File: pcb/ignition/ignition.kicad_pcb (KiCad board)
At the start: 2 copper layers, 71 parts, among them IC1 LTC4151, IC2 LTC4151, IC3 LTC4151, IC4 LTC4151, IC5 LTC4151, IC6 LTC4151, IC7 STM32F4xxVxTx, J1 PSU, J2 PSU, J3 CH2, J4 CH4, J5 CH1, J6 CH3, J7 CH5, Q1 NFET, Q2 NFET, Q3 NFET, Q4 NFET, Q5 NFET, Q6 NFET

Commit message: finished schematic
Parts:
- added C1: 10u, agg:1206, F.Cu at (67.4, -17.0)
- added C10: 100n, agg:0402, F.Cu at (122.8, -16.2)
- added C11: 100n, agg:0402, F.Cu at (149.0, -34.7)
- added C12: 1µ, agg:0402, F.Cu at (145.2, -29.2)
- added C13: 100n, agg:0402, F.Cu at (149.0, -33.5)
- added C14: 100n, agg:0402, F.Cu at (145.9, -30.5)
- added C15: 100n, agg:0402, F.Cu at (152.1, -37.1)
- added C16: 100n, agg:0402, F.Cu at (134.6, -18.9)
- added C17: 2µ2, agg:0402, F.Cu at (140.6, -42.2)
- added C18: 2µ2, agg:0402, F.Cu at (155.8, -40.6)
- added C19: 100n, agg:0402, F.Cu at (120.7, -16.2)
- added C2: 10u, agg:1206, F.Cu at (72.1, -17.0)
- added C20: 100n, agg:0402, F.Cu at (118.6, -16.2)
- added C3: 1u, agg:0603-L, F.Cu at (140.7, -44.5)
- added C4: 10n, agg:0603-L, F.Cu at (140.7, -43.4)
- added C5: 1u, agg:0603-L, F.Cu at (122.7, -35.2)
- added C6: 10p, agg:0402, F.Cu at (124.9, -16.2)
- added C7: 10p, agg:0402, F.Cu at (127.0, -16.2)
- added C8: 4µ7, agg:0402, F.Cu at (129.2, -16.2)
- added C9: 100n, agg:0402, F.Cu at (145.9, -31.7)
- added D12: D, ignition:SOD-123F, F.Cu at (137.5, -45.0)
- added D13: D, ignition:SOD-123F, F.Cu at (137.5, -42.7)
- added IC8: STM32F437VIT6, agg:LQFP-100, F.Cu at (88.0, 42.0)
- added J10: CH2, ignition:172316-1104, F.Cu at (54.0, 114.0)
- added J11: CH4, ignition:172316-1104, F.Cu at (94.0, 114.0)
- added J12: ARM, agg:S02B-PASK-2, F.Cu at (111.0, 42.0)
- added J13: UART1, agg:S03B-PASK-2, F.Cu at (111.0, 34.0)
- added J14: UART2, agg:S03B-PASK-2, F.Cu at (111.0, 25.0)
- added J15: CH1, ignition:172316-1104, F.Cu at (34.0, 114.0)
- added J16: CH3, ignition:172316-1104, F.Cu at (74.0, 114.0)
- added J17: CH5, ignition:172316-1104, F.Cu at (114.0, 114.0)
- added J8: LED4, agg:S02B-PASK-2, F.Cu at (85.0, 111.0)
- added J9: LED5, agg:S02B-PASK-2, F.Cu at (105.0, 111.0)
- added K1: 16A SPST, ignition:RT33L024, F.Cu at (68.0, -56.0)
- added K2: 16A SPST, ignition:RT33L024, F.Cu at (99.0, -69.5)
- added K3: 16A SPST, ignition:RT33L024, F.Cu at (68.0, -42.5)
- added K4: 16A SPST, ignition:RT33L024, F.Cu at (99.0, -56.0)
- added K5: 16A SPST, ignition:RT33L024, F.Cu at (68.0, -69.5)
- added K6: 16A SPST, ignition:RT33L024, F.Cu at (53.0, -77.0)
- added P1: SWD_TC, agg:TC2030-NL, F.Cu at (92.2, -24.0)
- added R41: 1k, agg:0603, F.Cu at (135.1, -21.7)
- added R42: 100R, agg:0603, F.Cu at (153.2, -40.0)
- added R43: 100R, agg:0603, F.Cu at (132.0, -20.2)
- added R44: 100R, agg:0603, F.Cu at (132.0, -18.7)
- added R45: 1k, agg:0603, F.Cu at (160.0, -48.0)
- added R46: 100R, agg:0603, F.Cu at (174.7, -62.5)
- added R47: 1k, agg:0603, F.Cu at (135.1, -20.2)
- added R48: 1k, agg:0603, F.Cu at (132.0, -17.2)
- added R49: 1k, agg:0603, F.Cu at (156.9, -42.0)
- added R50: 1k, agg:0603, F.Cu at (160.0, -45.0)
- added R51: 1k, agg:0603, F.Cu at (138.9, -24.0)
- added R52: 10k, agg:0603, F.Cu at (142.6, -27.5)
- added R53: 10k, agg:0603, F.Cu at (138.9, -25.5)
- added R54: 10k, agg:0603, F.Cu at (174.7, -67.0)
- added R55: 47k, agg:0603-L, F.Cu at (140.7, -45.6)
- added R56: 47k, agg:0603-L, F.Cu at (155.5, -62.1)
- added R57: 47k, agg:0603-L, F.Cu at (155.5, -63.2)
- added R58: 47k, agg:0603-L, F.Cu at (155.7, -64.3)
- added R59: 47k, agg:0603-L, F.Cu at (114.2, -16.3)
- added R60: 100, agg:0402, F.Cu at (116.5, -16.2)
- added TP1: TESTPAD, agg:TESTPAD, F.Cu at (136.3, -40.7)
- added TP2: TESTPAD, agg:TESTPAD, F.Cu at (179.1, -79.2)
- added TP3: TESTPAD, agg:TESTPAD, F.Cu at (129.5, -35.1)
- added TP4: TESTPAD, agg:TESTPAD, F.Cu at (179.1, -76.2)
- added TP5: TESTPAD, agg:TESTPAD, F.Cu at (179.1, -77.7)
- added U1: MICROSD, agg:MICROSD_MOLEX_503398-1892, F.Cu at (134.4, -69.2)
- added X33: Hole, agg:M3_MOUNT, F.Cu at (133.8, -36.2)
- added X34: Hole, agg:M3_MOUNT, F.Cu at (152.0, -45.6)
- added X35: Hole, agg:M3_MOUNT, F.Cu at (133.8, -29.4)
- added X36: Hole, agg:M3_MOUNT, F.Cu at (160.5, -52.2)
- added Y1: 26M, agg:XTAL-20x16, F.Cu at (155.7, -66.3)
- D10, D9: value D -> LED; footprint ignition:SOD-123F -> agg:0603-LED
- IC7: value STM32F4xxVxTx -> ADP3335; footprint agg:LQFP-100 -> agg:MSOP-8
- J1: footprint agg:S03B-PASK-2 -> ignition:172316-1104
- J2: value PSU -> LED1; footprint agg:S03B-PASK-2 -> agg:S02B-PASK-2
- J3: value CH2 -> PSU; footprint agg:S02B-PASK-2 -> ignition:172316-1104
- J4: value CH4 -> LED2
- J5: value CH1 -> 5v In
- J6: value CH3 -> 5v Out
- J7: value CH5 -> LED3
- R1, R4: value 10k -> 56R
- R11: value 100R -> 10k
- R12: value 110k -> 56R
- R13: value 110k -> 0.01R; footprint agg:0603 -> agg:2512
- R14, R15, R34: value 100R -> 110k
- R16, R35, R36: value 1k -> 110k
- R17: value 1k -> 56R
- R18, R19, R21: value 10k -> 100R
- R2: value 0.01R -> 10k; footprint agg:2512 -> agg:0603
- R20, R38, R39, R40: value 10k -> 110k
- R22: value 10k -> 1k
- R23: value 0.05R -> 1k; footprint agg:2512 -> agg:0603
- R24: value 0.05R -> 56R; footprint agg:2512 -> agg:0603
- R25, R6: value 0.05R -> 10k; footprint agg:2512 -> agg:0603
- R26, R28, R29, R30: value 110k -> 10k
- R27: value 110k -> 100R
- R31, R8: value 110k -> 0.05R; footprint agg:0603 -> agg:2512
- R32, R33: value 100R -> 0.05R; footprint agg:0603 -> agg:2512
- R37: value 1k -> 100R
- moved R25 136.1 mm to (177.9, -67.0)
- moved R10 135.3 mm to (171.6, -65.5)
- moved R1 133.6 mm to (177.9, -64.0)
- moved R24 131.0 mm to (171.6, -61.0)
- moved R26 127.9 mm to (171.6, -59.5)
- moved R34 125.7 mm to (174.7, -61.0)
- moved R30 122.4 mm to (171.6, -58.0)
- moved R3 122.2 mm to (171.6, -64.0)
- moved R4 119.2 mm to (171.6, -62.5)
- moved R39 119.0 mm to (177.9, -65.5)
- moved IC6 118.9 mm to (152.4, -65.9)
- moved D3 117.6 mm to (123.7, -51.8)
- moved R11 117.5 mm to (165.4, -53.3)
- moved R18 116.1 mm to (171.6, -67.0)
- moved R28 114.9 mm to (168.5, -54.8)
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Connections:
- net Net-(D2-Pad2) renamed /LED4
- net Net-(D8-Pad2) renamed /LED5
- D1 pad 2: Net-(D1-Pad2) -> /LED2
- D10 pad 1: 3v3 -> GND
- D10 pad 2: /CH3_CONT -> Net-(D10-Pad2)
- D11 pad 2: /CH5_CONT -> /CH1_CONT
- D6 pad 2: Net-(D6-Pad2) -> /LED1
- D7 pad 2: Net-(D7-Pad2) -> /LED3
- D9 pad 1: 3v3 -> GND
- D9 pad 2: /CH1_CONT -> Net-(D9-Pad2)
- IC1 pad 1: VCC -> /FIRE_DIST
- IC1 pad 2: VCC -> /FIRE_DIST
- IC1 pad 3: GND -> /FIRE_DIST
- IC1 pad 4: GND -> /FIRE_DIST
- IC1 pad 6: /I2C1_SCL -> /I2C2_SCL
- IC1 pad 7: /I2C1_SDA -> /I2C2_SDA
- IC2 pad 3: Net-(IC2-Pad3) -> GND
- IC2 pad 4: Net-(IC2-Pad4) -> /FIRE_DIST
- IC2 pad 6: /I2C1_SCL -> /I2C2_SCL
- IC2 pad 7: /I2C1_SDA -> /I2C2_SDA
- IC3 pad 1: /FIRE_DIST -> VCC
- IC3 pad 2: /FIRE_DIST -> VCC
- IC3 pad 3: Net-(IC3-Pad3) -> GND
- IC3 pad 4: Net-(IC3-Pad4) -> GND
- IC4 pad 3: /FIRE_DIST -> GND
- IC4 pad 6: /I2C1_SCL -> /I2C2_SCL
- IC4 pad 7: /I2C1_SDA -> /I2C2_SDA
- IC5 pad 3: Net-(IC5-Pad3) -> /FIRE_DIST
- IC5 pad 4: Net-(IC5-Pad4) -> GND
- IC5 pad 6: /I2C1_SCL -> /I2C2_SCL
- IC5 pad 7: /I2C1_SDA -> /I2C2_SDA
- IC6 pad 4: Net-(IC6-Pad4) -> GND
- IC6 pad 6: /I2C1_SCL -> /I2C2_SCL
- IC6 pad 7: /I2C1_SDA -> /I2C2_SDA
- IC7 pad 1: Net-(IC7-Pad1) -> 3v3
- IC7 pad 2: Net-(IC7-Pad2) -> 3v3
- IC7 pad 3: Net-(IC7-Pad3) -> 3v3
- IC7 pad 4: Net-(IC7-Pad4) -> GND
- IC7 pad 6: Net-(IC7-Pad6) -> 5v
- IC7 pad 7: Net-(IC7-Pad7) -> 5v
- IC7 pad 8: Net-(IC7-Pad8) -> 5v
- J2 pad 1: GND -> Net-(J2-Pad1)
- J2 pad 2: GND -> /LED1
- J3 pad 1: /CH2 -> GND
- J4 pad 1: /CH4 -> Net-(J4-Pad1)
- J4 pad 2: GND -> /LED2
- J5 pad 1: /CH1 -> 5v
- J6 pad 1: /CH3 -> 5v
- J7 pad 1: /CH5 -> Net-(J7-Pad1)
- J7 pad 2: GND -> /LED3
- Q1 pad 3: Net-(D1-Pad2) -> /LED2
- Q4 pad 3: Net-(D6-Pad2) -> /LED1
- Q5 pad 3: Net-(D7-Pad2) -> /LED3
- R1 pad 1: GND -> Net-(J2-Pad1)
- R1 pad 2: Net-(IC1-Pad5) -> 3v3
- R10 pad 1: GND -> /CH4
- R10 pad 2: Net-(Q1-Pad1) -> Net-(IC2-Pad5)
- R11 pad 1: /ARM_SUPPLY -> GND
- R11 pad 2: Net-(Q1-Pad1) -> Net-(IC3-Pad5)
- R12 pad 1: GND -> Net-(J7-Pad1)
- R12 pad 2: Net-(Q2-Pad1) -> 3v3
- R13 pad 1: GND -> Net-(D3-Pad1)
- R13 pad 2: Net-(Q3-Pad1) -> VCC
- R14 pad 1: /CH2_FIRE -> /FIRE_DIST
- R14 pad 2: Net-(Q2-Pad1) -> Net-(IC3-Pad5)
- R15 pad 1: /CH4_FIRE -> GND
- R15 pad 2: Net-(Q3-Pad1) -> Net-(Q1-Pad1)
- R16 pad 1: /CH2 -> GND
- R16 pad 2: 3v3 -> Net-(Q2-Pad1)
- R17 pad 1: /CH4 -> Net-(J8-Pad1)
- R18 pad 1: /CH2 -> /CH2_FIRE
- R18 pad 2: /CH2_CONT -> Net-(Q1-Pad1)
- R19 pad 1: /CH4 -> /CH4_FIRE
- R19 pad 2: /CH4_CONT -> Net-(Q2-Pad1)
- R2 pad 1: Net-(D1-Pad1) -> /PSU_MON
- R2 pad 2: VCC -> GND
- R20 pad 2: Net-(IC4-Pad5) -> Net-(Q3-Pad1)
- R21 pad 1: GND -> /ARM_SUPPLY
- R21 pad 2: Net-(IC5-Pad5) -> Net-(Q3-Pad1)
- R22 pad 1: GND -> /CH2
- R22 pad 2: Net-(IC6-Pad5) -> 3v3
- R23 pad 1: Net-(D6-Pad1) -> /CH4
- R23 pad 2: /FIRE_DIST -> 3v3
- R24 pad 1: Net-(D7-Pad1) -> Net-(J9-Pad1)
- R24 pad 2: /FIRE_DIST -> 3v3
- R25 pad 1: Net-(D8-Pad1) -> /CH2
- R25 pad 2: /FIRE_DIST -> /CH2_CONT
- R26 pad 1: /CH1 -> /CH4
- R26 pad 2: Net-(IC4-Pad5) -> /CH4_CONT
- R27 pad 1: /CH3 -> Net-(J12-Pad1)
- R27 pad 2: Net-(IC5-Pad5) -> /ARM_GRN
- R28 pad 1: /CH5 -> GND
- R28 pad 2: Net-(IC6-Pad5) -> Net-(IC4-Pad5)
- R29 pad 2: Net-(Q4-Pad1) -> Net-(IC5-Pad5)
- R3 pad 1: /FIRE_DIST -> /PSU_MON
- R3 pad 2: Net-(IC1-Pad5) -> VCC
- R30 pad 2: Net-(Q5-Pad1) -> Net-(IC6-Pad5)
- R31 pad 1: GND -> Net-(D6-Pad1)
- R31 pad 2: Net-(Q6-Pad1) -> /FIRE_DIST
- R32 pad 1: /CH1_FIRE -> Net-(D7-Pad1)
- R32 pad 2: Net-(Q4-Pad1) -> /FIRE_DIST
- R33 pad 1: /CH3_FIRE -> Net-(D8-Pad1)
- R33 pad 2: Net-(Q5-Pad1) -> /FIRE_DIST
- R34 pad 1: /CH5_FIRE -> /CH1
- R34 pad 2: Net-(Q6-Pad1) -> Net-(IC4-Pad5)
- R35 pad 1: /CH1 -> /CH3
- R35 pad 2: 3v3 -> Net-(IC5-Pad5)
- R36 pad 1: /CH3 -> /CH5
- R36 pad 2: 3v3 -> Net-(IC6-Pad5)
- R37 pad 1: /CH5 -> 3v3
- R37 pad 2: 3v3 -> Net-(D9-Pad2)
- R38 pad 1: /CH1 -> GND
- R38 pad 2: /CH1_CONT -> Net-(Q4-Pad1)
- R39 pad 1: /CH3 -> GND
- R39 pad 2: /CH3_CONT -> Net-(Q5-Pad1)
- R4 pad 1: GND -> Net-(J4-Pad1)
- R4 pad 2: Net-(IC2-Pad5) -> 3v3
- R40 pad 1: /CH5 -> GND
- R40 pad 2: /CH5_CONT -> Net-(Q6-Pad1)
- R5 pad 2: Net-(IC3-Pad5) -> Net-(IC1-Pad5)
- R6 pad 1: Net-(D2-Pad1) -> GND
- R6 pad 2: /FIRE_DIST -> Net-(IC2-Pad5)
- R7 pad 1: Net-(D3-Pad1) -> Net-(D1-Pad1)
- R8 pad 1: /CH2 -> Net-(D2-Pad1)
- R8 pad 2: Net-(IC2-Pad5) -> /FIRE_DIST
- R9 pad 1: /CH4 -> /CH2
- R9 pad 2: Net-(IC3-Pad5) -> Net-(IC1-Pad5)
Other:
- board outline added: 100 x 100 mm

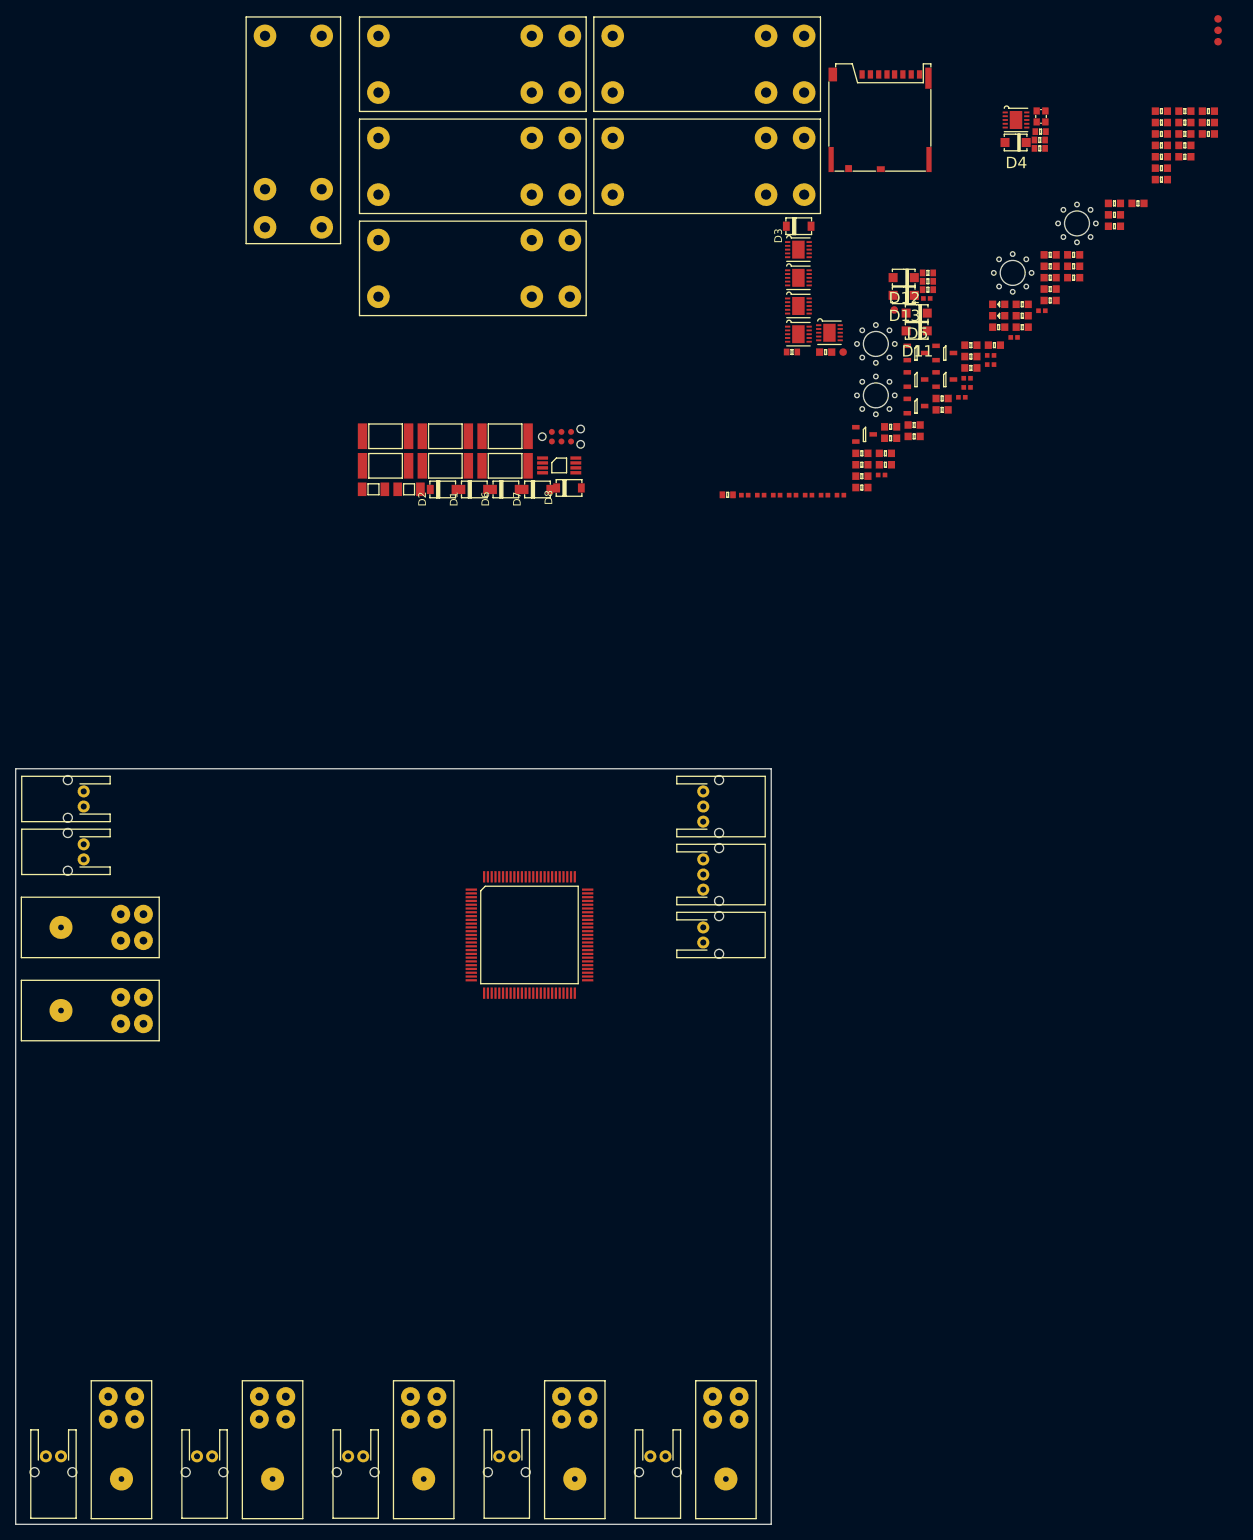
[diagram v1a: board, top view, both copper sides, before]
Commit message: finalised schematic, started pcb component placement
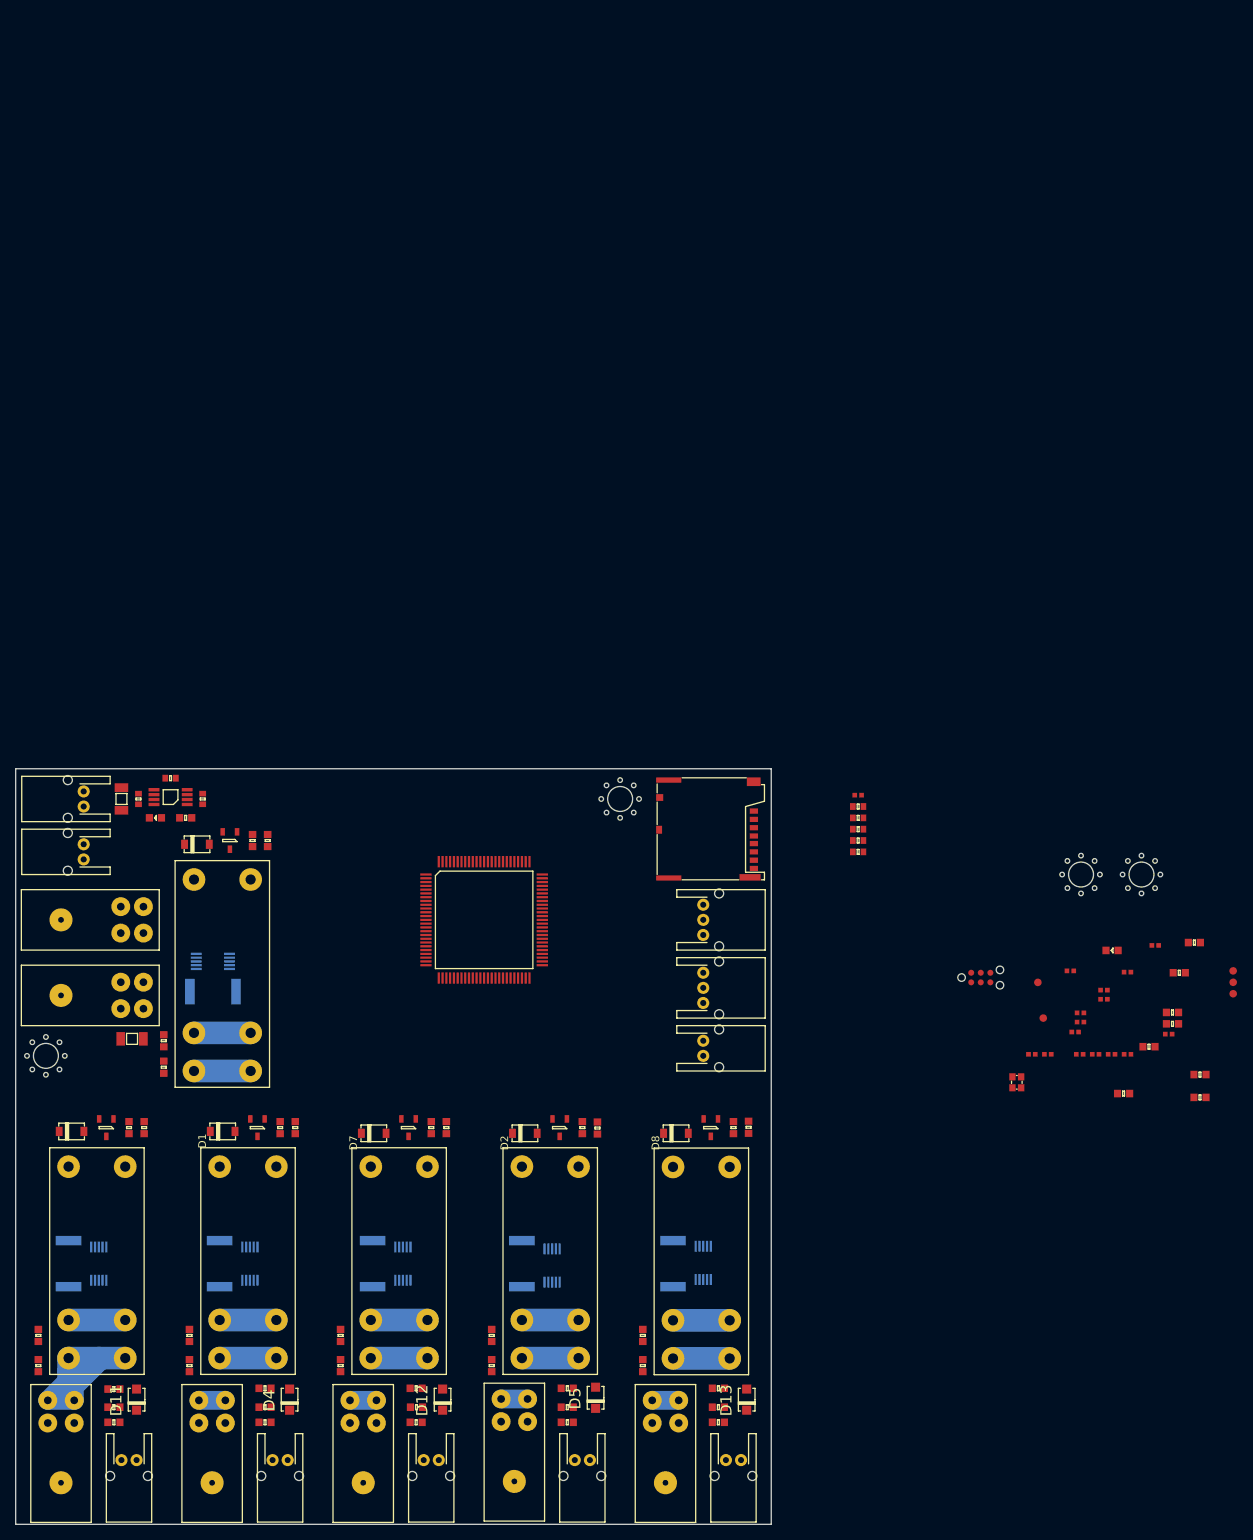
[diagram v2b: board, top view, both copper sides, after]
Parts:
- IC1, IC2, IC3, IC4, IC5, IC6: footprint agg:DFN-10-EP-LT -> agg:MSOP-10; moved to B.Cu
- R13, R31, R32, R33, R7, R8: moved to B.Cu
- moved R1 223.7 mm to (33.0, 106.5)
- moved R34 220.5 mm to (23.0, 99.0), turned to 90 degrees
- moved R25 210.1 mm to (53.0, 102.0)
- moved R28 208.9 mm to (23.0, 95.0), turned to 270 degrees
- moved R4 206.5 mm to (53.0, 106.5)
- moved D4 192.1 mm to (56.2, 103.5), turned to 270 degrees
- moved R49 191.9 mm to (33.0, 104.5)
- moved R23 187.3 mm to (93.0, 104.5)
- moved R10 186.9 mm to (83.0, 99.0), turned to 90 degrees
- moved R5 182.8 mm to (43.0, 95.0), turned to 270 degrees
- moved R54 180.0 mm to (113.0, 102.0)
- moved R26 179.6 mm to (93.0, 102.0)
- moved R24 177.5 mm to (113.0, 106.5)
- moved R18 176.8 mm to (57.0, 67.5), turned to 90 degrees
- moved X36 175.4 mm to (24.0, 58.0)
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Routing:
- net /CH1: track 0.00 -> 28.0 mm
- net /CH5: track 0.00 -> 11.0 mm
- net /CH4: track 0.00 -> 11.0 mm
- net /CH3: track 0.00 -> 11.0 mm
- net /CH2: track 0.00 -> 11.0 mm
- net Net-(D8-Pad1): track 0.00 -> 7.50 mm
- net Net-(D7-Pad1): track 0.00 -> 7.50 mm
- net Net-(D6-Pad1): track 0.00 -> 7.50 mm
- net Net-(D3-Pad1): track 0.00 -> 7.50 mm
- net Net-(D2-Pad1): track 0.00 -> 7.50 mm
- net Net-(D1-Pad1): track 0.00 -> 7.50 mm
- net /FIRE_DIST: track 0.00 -> 7.50 mm
- added copper zone on In2.Cu, net GND
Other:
- copper layers 2 -> 4
- rule pad_to_mask_clearance: 0.051 -> 0
- rule trace_min: 0.2 -> 0.15
- rule via_min_drill: 0.3 -> 0.4
- rule via_min_size: 0.4 -> 0.6

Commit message: ignition pcb almost complete
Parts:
- C1: moved to B.Cu
- moved R2 141.6 mm to (35.2, 57.4), turned to 180 degrees
- moved X33 132.7 mm to (40.8, 90.0)
- moved R3 131.6 mm to (35.2, 55.8), turned to 180 degrees
- moved R47 117.2 mm to (57.4, 35.4), turned to 225 degrees
- moved R48 111.6 mm to (60.0, 37.7), turned to 225 degrees
- moved C16 104.2 mm to (69.0, 43.6)
- moved C7 102.3 mm to (64.4, 39.2), turned to 270 degrees
- moved C8 100.7 mm to (69.0, 35.5)
- moved C6 96.0 mm to (68.8, 38.8), turned to 90 degrees
- moved C13 96.0 mm to (69.0, 37.0)
- moved C11 92.8 mm to (73.7, 28.2), turned to 270 degrees
- moved C9 92.5 mm to (69.0, 42.4)
- moved C12 91.8 mm to (69.0, 44.8)
- moved R60 89.5 mm to (66.6, 41.0)
- moved C20 89.2 mm to (69.0, 41.2)
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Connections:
- D1 pad 1: Net-(D1-Pad1) -> /FIRE_DIST
- D2 pad 1: Net-(D2-Pad1) -> /FIRE_DIST
- D3 pad 1: Net-(D3-Pad1) -> VCC
- D6 pad 1: Net-(D6-Pad1) -> /FIRE_DIST
- D7 pad 1: Net-(D7-Pad1) -> /FIRE_DIST
- D8 pad 1: Net-(D8-Pad1) -> /FIRE_DIST
- IC1 pad 10: Net-(D1-Pad1) -> Net-(IC1-Pad10)
- IC2 pad 10: Net-(D2-Pad1) -> Net-(IC2-Pad10)
- IC3 pad 10: Net-(D3-Pad1) -> Net-(IC3-Pad10)
- IC4 pad 10: Net-(D6-Pad1) -> Net-(IC4-Pad10)
- IC5 pad 10: Net-(D7-Pad1) -> Net-(IC5-Pad10)
- IC6 pad 10: Net-(D8-Pad1) -> Net-(IC6-Pad10)
- IC8 pad 1: Net-(IC8-Pad1) -> /ARM_SUPPLY
- IC8 pad 24: Net-(IC8-Pad24) -> /PSU_MON
- IC8 pad 34: /PSU_MON -> Net-(IC8-Pad34)
- IC8 pad 36: Net-(IC8-Pad36) -> /CH1_FIRE
- IC8 pad 37: Net-(IC8-Pad37) -> /CH2_FIRE
- IC8 pad 38: Net-(IC8-Pad38) -> /CH3_FIRE
- IC8 pad 39: /ARM_GRN -> /CH4_FIRE
- IC8 pad 40: /ARM_RED -> /CH5_FIRE
- IC8 pad 43: /STATUS -> Net-(IC8-Pad43)
- IC8 pad 51: Net-(IC8-Pad51) -> /ARM_GRN
- IC8 pad 52: Net-(IC8-Pad52) -> /ARM_RED
- IC8 pad 55: /ARM_SUPPLY -> Net-(IC8-Pad55)
- IC8 pad 56: /CH1_FIRE -> Net-(IC8-Pad56)
- IC8 pad 57: /CH2_FIRE -> Net-(IC8-Pad57)
- IC8 pad 58: /CH3_FIRE -> Net-(IC8-Pad58)
- IC8 pad 59: /CH4_FIRE -> Net-(IC8-Pad59)
- IC8 pad 60: /CH5_FIRE -> Net-(IC8-Pad60)
- IC8 pad 64: Net-(IC8-Pad64) -> /STATUS
- K1 pad 2: Net-(D1-Pad1) -> /FIRE_DIST
- K1 pad 3: Net-(D1-Pad1) -> Net-(IC1-Pad10)
- K2 pad 2: Net-(D2-Pad1) -> /FIRE_DIST
- K2 pad 3: Net-(D2-Pad1) -> Net-(IC2-Pad10)
- K3 pad 2: Net-(D3-Pad1) -> VCC
- K3 pad 3: Net-(D3-Pad1) -> Net-(IC3-Pad10)
- K4 pad 2: Net-(D6-Pad1) -> /FIRE_DIST
- K4 pad 3: Net-(D6-Pad1) -> Net-(IC4-Pad10)
- K5 pad 2: Net-(D7-Pad1) -> /FIRE_DIST
- K5 pad 3: Net-(D7-Pad1) -> Net-(IC5-Pad10)
- K6 pad 2: Net-(D8-Pad1) -> /FIRE_DIST
- K6 pad 3: Net-(D8-Pad1) -> Net-(IC6-Pad10)
- R13 pad 1: Net-(D3-Pad1) -> Net-(IC3-Pad10)
- R31 pad 1: Net-(D6-Pad1) -> Net-(IC4-Pad10)
- R32 pad 1: Net-(D7-Pad1) -> Net-(IC5-Pad10)
- R33 pad 1: Net-(D8-Pad1) -> Net-(IC6-Pad10)
- R7 pad 1: Net-(D1-Pad1) -> Net-(IC1-Pad10)
- R8 pad 1: Net-(D2-Pad1) -> Net-(IC2-Pad10)
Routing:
- net 3v3: track 0.00 -> 216.5 mm, vias 0 -> 16
- net GND: track 0.00 -> 164.6 mm, vias 0 -> 75
- net /I2C2_SDA: track 0.00 -> 144.7 mm, vias 0 -> 9
- net /I2C2_SCL: track 0.00 -> 141.2 mm, vias 0 -> 9
- net /FIRE_DIST: track 7.50 -> 129.5 mm, vias 0 -> 1
- net /CH1_CONT: track 0.00 -> 96.7 mm, vias 0 -> 4
- net /CH5_CONT: track 0.00 -> 94.5 mm, vias 0 -> 2
- net /CH4_CONT: track 0.00 -> 85.9 mm, vias 0 -> 4
- net /CH2_CONT: track 0.00 -> 76.3 mm, vias 0 -> 4
- net /CH3_CONT: track 0.00 -> 71.2 mm, vias 0 -> 4
- net VCC: track 0.00 -> 60.0 mm
- net /CH1_FIRE: track 0.00 -> 55.8 mm, vias 0 -> 2
- net /CH5_FIRE: track 0.00 -> 53.5 mm
- net /LED1: track 0.00 -> 49.7 mm
- net /LED5: track 0.00 -> 49.6 mm
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- added copper zone on B.Cu, net /CH1
- added copper zone on B.Cu, net /CH2
- added copper zone on B.Cu, net /CH3
- added copper zone on B.Cu, net /CH4
- added copper zone on B.Cu, net /CH5
- added copper zone on B.Cu, net /FIRE_DIST
- added copper zone on B.Cu, net 3v3
- added copper zone on B.Cu, net GND
- added copper zone on In1.Cu, net GND
- added copper zone on B.Cu, net Net-(IC1-Pad10)
- added copper zone on B.Cu, net Net-(IC2-Pad10)
- added copper zone on B.Cu, net Net-(IC3-Pad10)
- added copper zone on B.Cu, net Net-(IC4-Pad10)
- added copper zone on B.Cu, net Net-(IC5-Pad10)
- added copper zone on B.Cu, net Net-(IC6-Pad10)
- added copper zone on B.Cu, net VCC
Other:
- rule trace_min: 0.15 -> 0.2

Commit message: pcb routing finished
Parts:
- moved TP1 136.5 mm to (45.5, 28.1)
- moved TP4 126.1 mm to (56.0, 34.0)
- moved TP5 119.3 mm to (62.4, 36.2)
- moved TP2 98.6 mm to (82.8, 54.1), turned to 270 degrees
- moved TP3 95.4 mm to (86.2, 54.1), turned to 270 degrees
- moved R59 49.9 mm to (81.7, 27.3), turned to 270 degrees
- moved R58 48.0 mm to (83.5, 27.2), turned to 270 degrees
- moved R57 46.4 mm to (85.2, 27.2), turned to 270 degrees
- moved R55 31.2 mm to (100.7, 31.3), turned to 180 degrees
- moved R56 31.1 mm to (100.7, 34.0), turned to 180 degrees
- moved C19 28.8 mm to (105.7, 36.2)
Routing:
- net /SDIO_CMD: track 0.00 -> 45.2 mm, vias 0 -> 2
- net /SDIO_D3: track 0.00 -> 44.8 mm, vias 0 -> 2
- net /SDIO_D2: track 0.00 -> 42.9 mm, vias 0 -> 2
- net /SDIO_CK: track 0.00 -> 39.2 mm, vias 0 -> 2
- net /SDIO_D0: track 0.00 -> 35.0 mm, vias 0 -> 2
- net /SDIO_D1: track 0.00 -> 33.2 mm, vias 0 -> 2
- net GND: track 164.6 -> 185.4 mm, vias 75 -> 84
- net 3v3: track 216.5 -> 227.3 mm, vias 16 -> 21
- net /I2C1_SCL: track 37.4 -> 39.7 mm
- net /I2C1_SDA: track 36.6 -> 38.9 mm
- net /I2C2_SCL: track 141.2 -> 142.7 mm
- net /I2C2_SDA: track 144.7 -> 146.2 mm
